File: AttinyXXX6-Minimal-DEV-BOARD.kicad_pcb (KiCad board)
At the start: 2 copper layers, 32.7 x 15.5 mm, 15 parts, among them J1 USB_B_Micro, J2 PWR_CONN, J3 UPDI, J4 Conn, J5 Conn, SW1 SW, U1 ATtinyXXX6

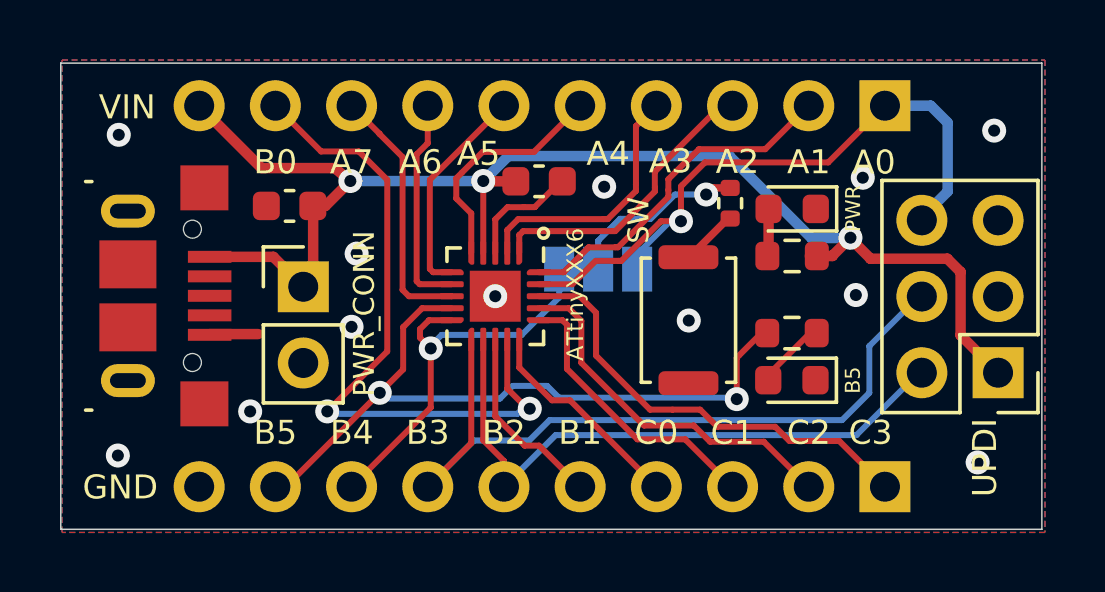
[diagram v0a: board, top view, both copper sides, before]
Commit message: pinout and updi
PIN B0 location change and UPDI connector pin change to universal one.
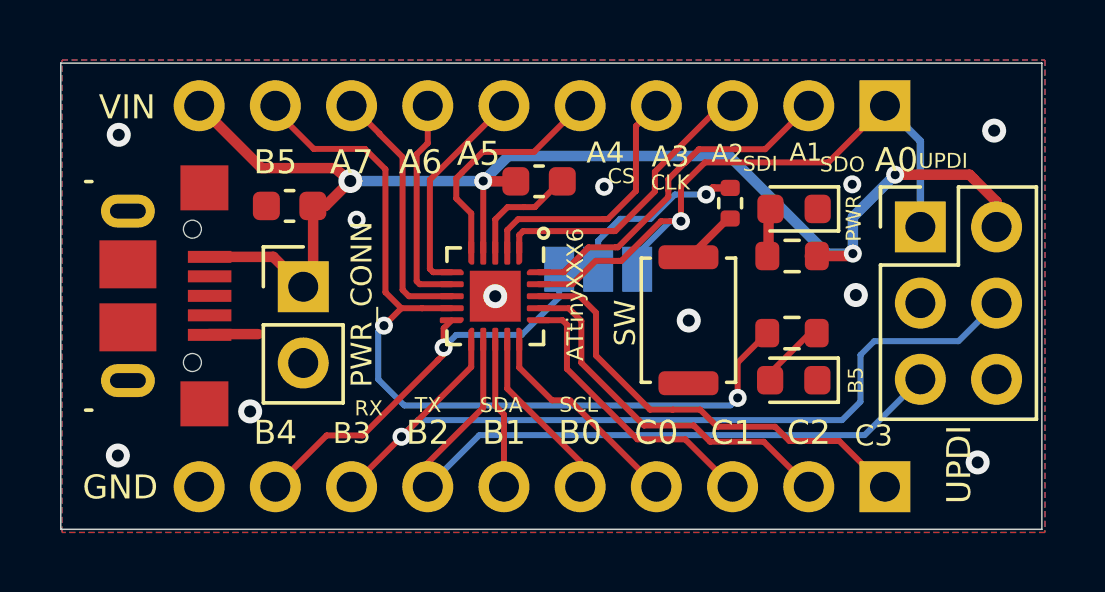
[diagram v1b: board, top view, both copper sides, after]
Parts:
- moved J3 5.51 mm to (139.5, 68.2), turned to 0 degrees
- moved D1 0.06 mm to (135.3, 67.5)
- moved D2 0.06 mm to (135.3, 73.3)
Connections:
- J3 pad 1: /VCC -> /A0
- J3 pad 2: /B2 -> /VCC
- J3 pad 3: GND -> unconnected-(J3-Pad3)
- J3 pad 5: GND -> /B2
- J3 pad 6: /A0 -> GND
- J4 pad 9: /B0 -> /B5
- J5 pad 5: /B1 -> /B0
- J5 pad 6: /B2 -> /B1
- J5 pad 7: /B3 -> /B2
- J5 pad 8: /B4 -> /B3
- J5 pad 9: /B5 -> /B4
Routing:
- net /B0: track 22.8 -> 5.91 mm, vias 2 -> 0
- net /B5: track 24.3 -> 28.9 mm
- net /B3: track 25.6 -> 29.1 mm, vias 0 -> 1
- net /B2: track 20.7 -> 23.6 mm
- net /B1: track 6.35 -> 5.02 mm
- net /A0: track 22.9 -> 21.6 mm
- net /B4: track 13.7 -> 14.2 mm
- net /VCC: track 45.2 -> 45.1 mm, vias 3 -> 4
- net GND: vias 12 -> 11
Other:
- board text added: "CLK"
- board text added: "CLK1"
- board text added: "CS"
- board text added: "CS1"
- board text added: "RX"
- board text added: "RX1"
- board text added: "SCL"
- board text added: "SCL1"
- board text added: "SDA"
- board text added: "SDA1"
- board text added: "SDI"
- board text added: "SDI1"
- board text added: "SDO"
- board text added: "SDO1"
- board text added: "TX"
- board text added: "TX1"
- board text added: "V0.0.2"
- board text removed: "V0.1"
